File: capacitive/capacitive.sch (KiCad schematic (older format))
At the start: 66 parts, among them J101 UL, J102 UART, J103 SWD, J104 TX_PADS, J105 RX_PAD, J106 POWER, J107 UR, J108 LL, J109 LR, Q101 RU1C002ZPTCL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

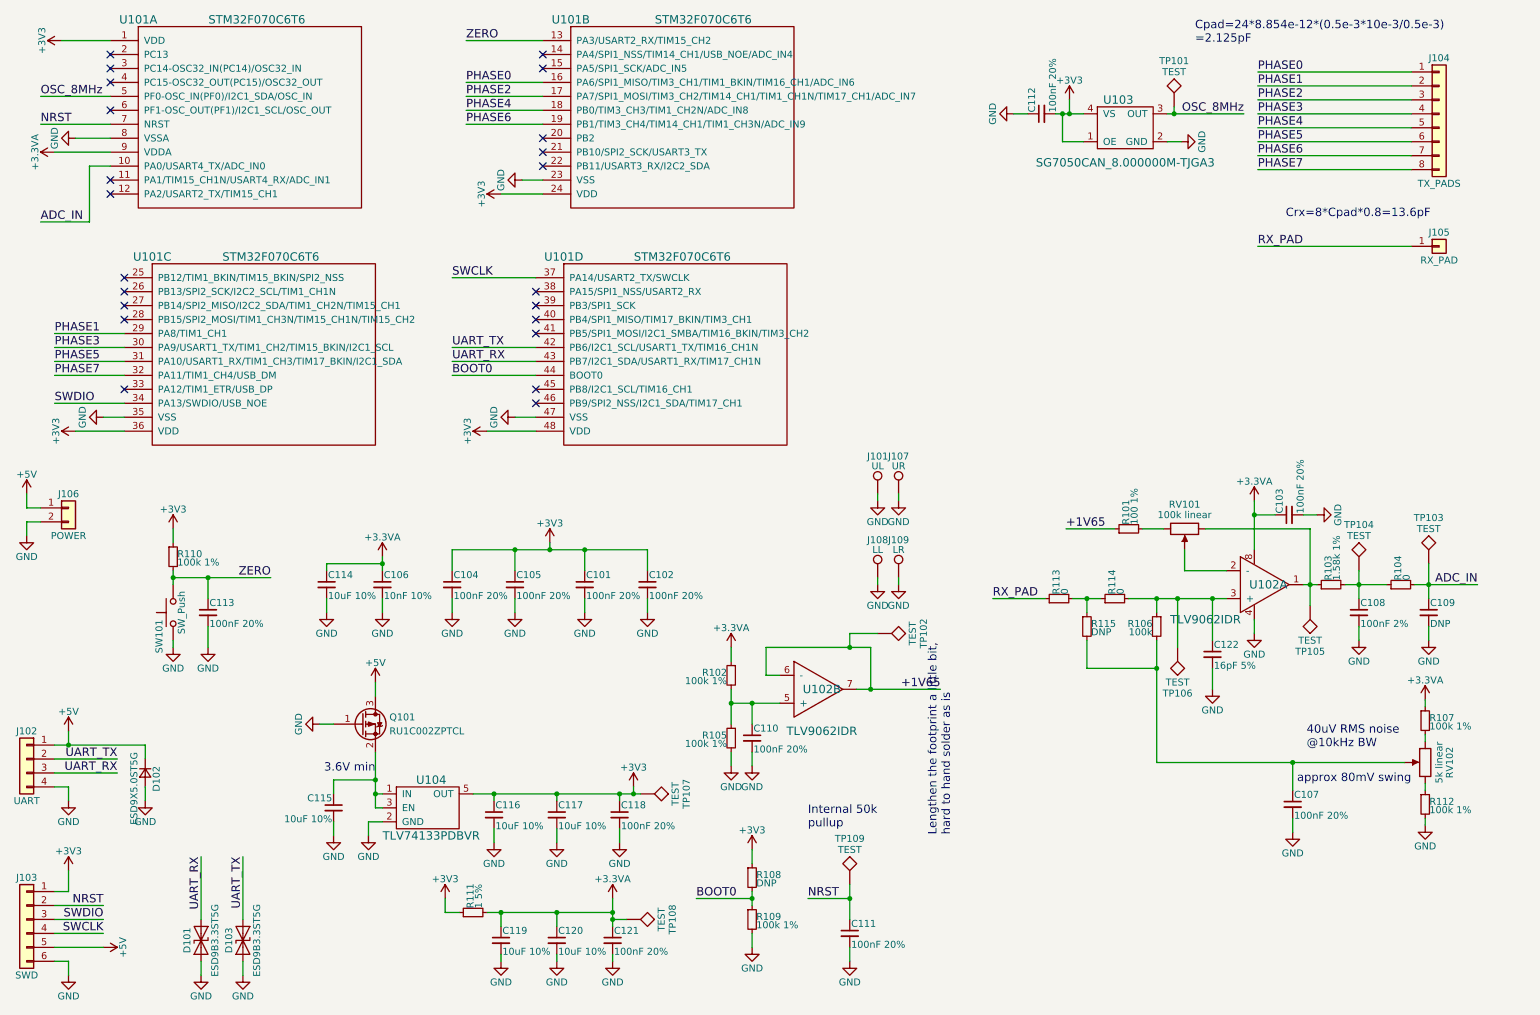
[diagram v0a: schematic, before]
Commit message: Add second stage of filtering
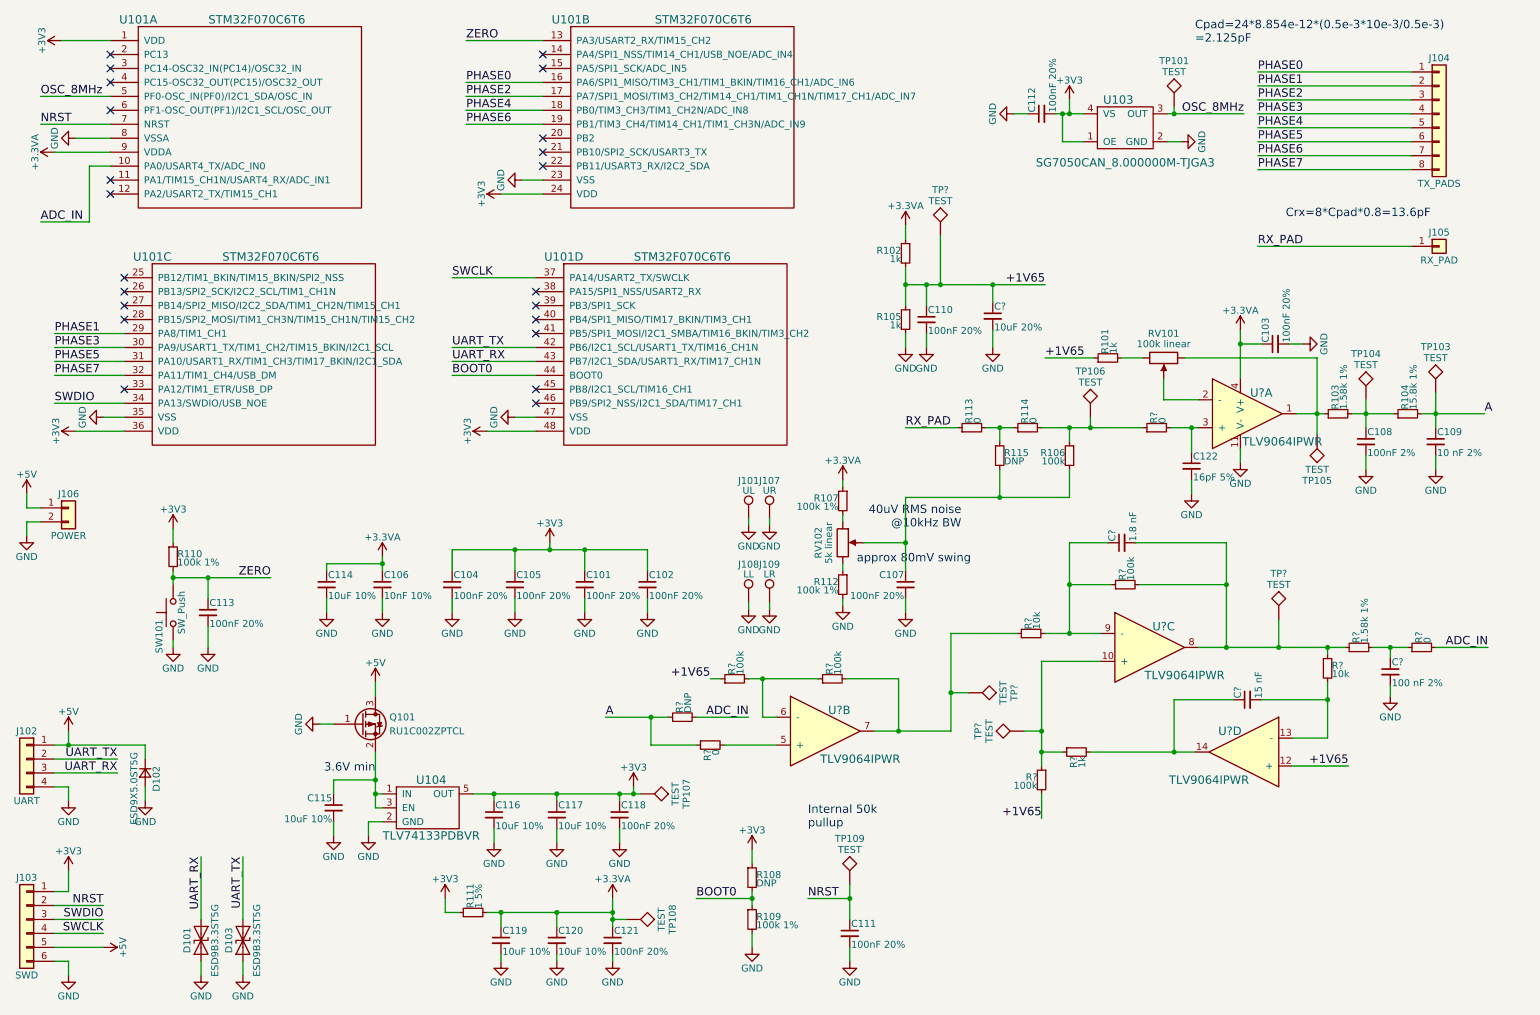
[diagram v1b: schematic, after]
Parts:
- removed TP102: TEST, Measurement_Points:Measurement_Point_Round-SMD-Pad_Small, symbol TEST
- removed U102: TLV9062IDR, capacitive:TI_SOIC-8, symbol TLV9062IDR
- added C?: 1.8 nF, symbol C_Small
- added C?: 15 nF, symbol C_Small
- added C?: 100 nF 2%, symbol C_Small
- added C?: 10uF 20%, Capacitors_SMD:C_0805_HandSoldering, symbol C_Small
- added R?: 0, Resistors_SMD:R_0805_HandSoldering, symbol R_Small
- added R?: 1k, symbol R_Small
- added R? (x4): 100k, symbol R_Small
- added R? (x2): 10k, symbol R_Small
- added R?: 1.58k 1%, symbol R_Small
- added R? (x2): 0, symbol R_Small
- added R?: DNP, symbol R_Small
- added TP?: TEST, symbol TEST
- added TP? (x3): TEST, Measurement_Points:Measurement_Point_Round-SMD-Pad_Small, symbol TEST
- added U? (x4): TLV9064IPWR, symbol TLV9064IPWR
- C109: value DNP -> 10 nF 2%
- R101: value 100 1% -> 1k
- R102, R105: value 100k 1% -> 1k
- R104: value 0 -> 15.8k 1%
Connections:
- net +1V65: now also C110.1, R102.2, R105.1, C?.1, R?.1, R?.2, TP?.1, U?.12 (+)
- net +3.3VA: now also U?.4 (V+)
- net ADC_IN: now also R?.2, R?.2; no longer C109.1, R104.2, TP103.1
- net GND: now also C?.2, C?.2, U?.11 (V-)
- net at R103.1, RV101.1, TP105.1: now also U?.1
- net at RV101.2: now also U?.2 (-)
- net at R106.1, R114.2, TP106.1: now also R?.1; no longer C122.1
- new net: C122.1, R?.2, U?.3 (+)
- new net: R?.2, U?.5 (+)
- new net: R?.1, R?.2, U?.6 (-)
- new net: R?.1, R?.2, TP?.1, U?.7
- new net: R?.1, R?.1, TP?.1, U?.10 (+)
- new net: C?.2, R?.1, R?.1, R?.2, TP?.1, U?.8
- new net: C?.1, R?.1, R?.2, U?.9 (-)
- new net: C?.2, R?.2, U?.13 (-)
- new net: C?.1, R?.2, U?.14
- new net: C?.1, R?.1, R?.2
- new net A: C109.1, R104.2, R?.1, R?.1, TP103.1
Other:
- note removed: "Lengthen the footprint a little bit,\nhard to hand solder as is"
- moved on the sheet: C103, C107, C108, C109, C110, C122, J101, J107, J108, J109, R101, R102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

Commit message: Save before autofill
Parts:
- C122: value 16pF 5% -> DNP; Mouser 81-GCM1885C1H160FA6J -> NoPart
- C123: renamed from C?; value 10uF 20% -> 10uF 10%
- R102, R105: value 1k -> 1k 1%; footprint Resistors_SMD:R_1206_HandSoldering -> Resistors_SMD:R_0402; Mouser 71-CRCW1206100KFKEAC -> 71-CRCW04021K00FKEDC
- R106: value 100k -> 100k 1%
- R117, R122, R123, R127: renamed from R?; value 100k -> 100k 1%
- R118: renamed from R?; value 10k -> 10k 1%; footprint (none) -> Resistors_SMD:R_0402; Mouser (none) -> 71-CRCW040210K0FKEDC
- R121: renamed from R?; value 10k -> 10k 1%
- R126: renamed from R?; value 1k -> 1k 1%
- U102: renamed from U?; footprint (none) -> capacitive:TI_TSSOP14; Mouser (none) -> 595-TLV9064IPWR
- gave numbers to parts that had none: 13
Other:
- note removed: "40uV RMS noise\n@10kHz BW"
- moved on the sheet: C124

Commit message: Autofill first time
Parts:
- R106, R117, R122, R123, R127: footprint (none) -> Resistors_SMD:R_1206_HandSoldering; Mouser (none) -> 71-CRCW1206100KFKEAC
- R108: Mouser (none) -> 71-RCS06030000Z0EA
- R119: footprint (none) -> Resistors_SMD:R_0603_HandSoldering; Mouser (none) -> 660-RN73H1JTD1581D25
- R120, R125: footprint (none) -> Resistors_SMD:R_0805_HandSoldering; Mouser (none) -> 71-CRCW12060000Z0EAC
- R121: footprint (none) -> Resistors_SMD:R_0402; Mouser (none) -> 71-CRCW040210K0FKEDC
- R124: footprint (none) -> Resistors_SMD:R_0603_HandSoldering; Mouser (none) -> 71-RCS06030000Z0EA
- R126: footprint (none) -> Resistors_SMD:R_0402; Mouser (none) -> 71-CRCW04021K00FKEDC
- TP102: footprint (none) -> Measurement_Points:Measurement_Point_Round-SMD-Pad_Small; Mouser (none) -> NoPart
- U102: footprint (none) -> capacitive:TI_TSSOP14; Mouser (none) -> 595-TLV9064IPWR
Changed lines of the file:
@@
 F 2 "Resistors_SMD:R_0603_HandSoldering" H 5850 6750 50  0001 C CNN
 F 3 "" H 5850 6750 50  0001 C CNN
+F 4 "71-RCS06030000Z0EA" H 5850 6750 50  0001 C "Mouser"
 	1    5850 6750
 	1    0    0    -1
@@
 F 0 "R106" H 8155 3745 50  0000 L CNN
 F 1 "100k 1%" H 8155 3685 50  0000 L CNN
-F 2 "" H 8125 3725 50  0001 C CNN
+F 2 "Resistors_SMD:R_1206_HandSoldering" H 8125 3725 50  0001 C CNN
 F 3 "" H 8125 3725 50  0001 C CNN
+F 4 "71-CRCW1206100KFKEAC" H 8125 3725 50  0001 C "Mouser"
 	1    8125 3725
 	1    0    0    -1
@@
 F 0 "TP102" H 7200 2450 50  0000 C BNN
 F 1 "TEST" H 7200 2400 50  0000 C CNN
-F 2 "" H 7200 2150 50  0001 C CNN
+F 2 "Measurement_Points:Measurement_Point_Round-SMD-Pad_Small" H 7200 2150 50  0001 C CNN
 F 3 "" H 7200 2150 50  0001 C CNN
+F 4 "NoPart" H 7200 2150 50  0001 C "Mouser"
 	1    7200 2150
 	1    0    0    -1
@@
 F 0 "U102" H 6475 5850 60  0000 C CNN
 F 1 "TLV9064IPWR" H 6625 5500 60  0000 C CNN
-F 2 "" H 6375 5700 60  0001 C CNN
+F 2 "capacitive:TI_TSSOP14" H 6375 5700 60  0001 C CNN
 F 3 "" H 6375 5700 60  0001 C CNN
+F 4 "595-TLV9064IPWR" H 6375 5700 60  0001 C "Mouser"
 	2    6375 5700
 	1    0    0    -1
@@
 F 0 "U102" H 8800 5250 60  0000 C CNN
 F 1 "TLV9064IPWR" H 8950 4900 60  0000 C CNN
-F 2 "" H 8700 5100 60  0001 C CNN
+F 2 "capacitive:TI_TSSOP14" H 8700 5100 60  0001 C CNN
 F 3 "" H 8700 5100 60  0001 C CNN
+F 4 "595-TLV9064IPWR" H 8700 5100 60  0001 C "Mouser"
 	3    8700 5100
 	1    0    0    -1
@@
 F 0 "R126" H 8205 5870 50  0000 L CNN
 F 1 "1k 1%" H 8205 5810 50  0000 L CNN
-F 2 "" H 8175 5850 50  0001 C CNN
+F 2 "Resistors_SMD:R_0402" H 8175 5850 50  0001 C CNN
 F 3 "" H 8175 5850 50  0001 C CNN
+F 4 "71-CRCW04021K00FKEDC" H 8175 5850 50  0001 C "Mouser"
 	1    8175 5850
 	0    -1   1    0
@@
 F 0 "R127" H 7955 6070 50  0000 L CNN
 F 1 "100k 1%" H 7955 6010 50  0000 L CNN
-F 2 "" H 7925 6050 50  0001 C CNN
+F 2 "Resistors_SMD:R_1206_HandSoldering" H 7925 6050 50  0001 C CNN
 F 3 "" H 7925 6050 50  0001 C CNN
+F 4 "71-CRCW1206100KFKEAC" H 7925 6050 50  0001 C "Mouser"
 	1    7925 6050
 	-1   0    0    -1
@@
 F 0 "R117" H 8555 4670 50  0000 L CNN
 F 1 "100k 1%" H 8555 4610 50  0000 L CNN
-F 2 "" H 8525 4650 50  0001 C CNN
+F 2 "Resistors_SMD:R_1206_HandSoldering" H 8525 4650 50  0001 C CNN
 F 3 "" H 8525 4650 50  0001 C CNN
+F 4 "71-CRCW1206100KFKEAC" H 8525 4650 50  0001 C "Mouser"
 	1    8525 4650
 	0    -1   -1   0
@@
 F 0 "U102" H 9475 6000 60  0000 C CNN
 F 1 "TLV9064IPWR" H 9625 5650 60  0000 C CNN
-F 2 "" H 9375 5850 60  0001 C CNN
+F 2 "capacitive:TI_TSSOP14" H 9375 5850 60  0001 C CNN
 F 3 "" H 9375 5850 60  0001 C CNN
+F 4 "595-TLV9064IPWR" H 9375 5850 60  0001 C "Mouser"
 	4    9375 5850
 	-1   0    0    -1
@@
 F 0 "R121" H 10005 5270 50  0000 L CNN
 F 1 "10k 1%" H 10005 5210 50  0000 L CNN
-F 2 "" H 9975 5250 50  0001 C CNN
+F 2 "Resistors_SMD:R_0402" H 9975 5250 50  0001 C CNN
 F 3 "" H 9975 5250 50  0001 C CNN
+F 4 "71-CRCW040210K0FKEDC" H 9975 5250 50  0001 C "Mouser"
 	1    9975 5250
 	1    0    0    -1
@@
 F 0 "R119" H 10230 5120 50  0000 L CNN
 F 1 "1.58k 1%" H 10230 5060 50  0000 L CNN
-F 2 "" H 10200 5100 50  0001 C CNN
+F 2 "Resistors_SMD:R_0603_HandSoldering" H 10200 5100 50  0001 C CNN
 F 3 "" H 10200 5100 50  0001 C CNN
+F 4 "660-RN73H1JTD1581D25" H 10200 5100 50  0001 C "Mouser"
 	1    10200 5100
 	0    -1   -1   0
@@
 F 0 "R125" H 5580 5820 50  0000 L CNN
 F 1 "0" H 5580 5760 50  0000 L CNN
-F 2 "" H 5550 5800 50  0001 C CNN
+F 2 "Resistors_SMD:R_0805_HandSoldering" H 5550 5800 50  0001 C CNN
 F 3 "" H 5550 5800 50  0001 C CNN
+F 4 "71-CRCW12060000Z0EAC" H 5550 5800 50  0001 C "Mouser"
 	1    5550 5800
 	0    -1   1    0
@@
 F 0 "R124" H 5380 5620 50  0000 L CNN
 F 1 "DNP" H 5380 5560 50  0000 L CNN
-F 2 "" H 5350 5600 50  0001 C CNN
+F 2 "Resistors_SMD:R_0603_HandSoldering" H 5350 5600 50  0001 C CNN
 F 3 "" H 5350 5600 50  0001 C CNN
+F 4 "71-RCS06030000Z0EA" H 5350 5600 50  0001 C "Mouser"
 	1    5350 5600
 	0    -1   -1   0
@@
 F 0 "R123" H 6455 5345 50  0000 L CNN
 F 1 "100k 1%" H 6455 5285 50  0000 L CNN
-F 2 "" H 6425 5325 50  0001 C CNN
+F 2 "Resistors_SMD:R_1206_HandSoldering" H 6425 5325 50  0001 C CNN
 F 3 "" H 6425 5325 50  0001 C CNN
+F 4 "71-CRCW1206100KFKEAC" H 6425 5325 50  0001 C "Mouser"
 	1    6425 5325
 	0    -1   -1   0
@@
 F 0 "R122" H 5755 5345 50  0000 L CNN
 F 1 "100k 1%" H 5755 5285 50  0000 L CNN
-F 2 "" H 5725 5325 50  0001 C CNN
+F 2 "Resistors_SMD:R_1206_HandSoldering" H 5725 5325 50  0001 C CNN
 F 3 "" H 5725 5325 50  0001 C CNN
+F 4 "71-CRCW1206100KFKEAC" H 5725 5325 50  0001 C "Mouser"
 	1    5725 5325
 	0    -1   -1   0
@@
 F 0 "R120" H 10680 5120 50  0000 L CNN
 F 1 "0" H 10680 5060 50  0000 L CNN
-F 2 "" H 10650 5100 50  0001 C CNN
+F 2 "Resistors_SMD:R_0805_HandSoldering" H 10650 5100 50  0001 C CNN
 F 3 "" H 10650 5100 50  0001 C CNN
+F 4 "71-CRCW12060000Z0EAC" H 10650 5100 50  0001 C "Mouser"
 	1    10650 5100
 	0    -1   -1   0

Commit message: Save before autofill
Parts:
- added C?: 33nF 5%, Capacitors_SMD:C_0603_HandSoldering, symbol C_Small
- C109: Mouser NoPart -> 81-GRM2195C1H103FA1D
- C124: value 1.8 nF -> 1.8nF 2%; footprint (none) -> Capacitors_SMD:C_0603_HandSoldering; Mouser (none) -> 81-GRM1885C1H182GA1D
- C125: value 100 nF 2% -> 100nF 2%
- C126: value 15 nF -> 33nF 5%
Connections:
- net at R126.2, U102.14: now also C?.1; no longer C126.1
- new net: C126.1, C?.2
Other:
- moved on the sheet: C126
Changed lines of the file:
@@
 F 2 "Capacitors_SMD:C_0805_HandSoldering" H 10750 3625 50  0001 C CNN
 F 3 "" H 10750 3625 50  0001 C CNN
-F 4 "NoPart" H 10750 3625 60  0001 C CNN "Mouser"
+F 4 "81-GRM2195C1H103FA1D" H 10750 3625 60  0001 C CNN "Mouser"
 	1    10750 3625
 	1    0    0    -1
@@
 F 2 "Resistors_SMD:R_0603_HandSoldering" H 5850 6750 50  0001 C CNN
 F 3 "" H 5850 6750 50  0001 C CNN
-F 4 "71-RCS06030000Z0EA" H 5850 6750 50  0001 C "Mouser"
+F 4 "71-RCS06030000Z0EA" H 5850 6750 50  0001 C CNN "Mouser"
 	1    5850 6750
 	1    0    0    -1
@@
 F 2 "Resistors_SMD:R_1206_HandSoldering" H 8125 3725 50  0001 C CNN
 F 3 "" H 8125 3725 50  0001 C CNN
-F 4 "71-CRCW1206100KFKEAC" H 8125 3725 50  0001 C "Mouser"
+F 4 "71-CRCW1206100KFKEAC" H 8125 3725 50  0001 C CNN "Mouser"
 	1    8125 3725
 	1    0    0    -1
@@
 F 2 "Measurement_Points:Measurement_Point_Round-SMD-Pad_Small" H 7200 2150 50  0001 C CNN
 F 3 "" H 7200 2150 50  0001 C CNN
-F 4 "NoPart" H 7200 2150 50  0001 C "Mouser"
+F 4 "NoPart" H 7200 2150 50  0001 C CNN "Mouser"
 	1    7200 2150
 	1    0    0    -1
@@
 F 2 "capacitive:TI_TSSOP14" H 6375 5700 60  0001 C CNN
 F 3 "" H 6375 5700 60  0001 C CNN
-F 4 "595-TLV9064IPWR" H 6375 5700 60  0001 C "Mouser"
+F 4 "595-TLV9064IPWR" H 6375 5700 60  0001 C CNN "Mouser"
 	2    6375 5700
 	1    0    0    -1
@@
 F 2 "capacitive:TI_TSSOP14" H 8700 5100 60  0001 C CNN
 F 3 "" H 8700 5100 60  0001 C CNN
-F 4 "595-TLV9064IPWR" H 8700 5100 60  0001 C "Mouser"
+F 4 "595-TLV9064IPWR" H 8700 5100 60  0001 C CNN "Mouser"
 	3    8700 5100
 	1    0    0    -1
@@
 F 2 "Resistors_SMD:R_0402" H 8175 5850 50  0001 C CNN
 F 3 "" H 8175 5850 50  0001 C CNN
-F 4 "71-CRCW04021K00FKEDC" H 8175 5850 50  0001 C "Mouser"
+F 4 "71-CRCW04021K00FKEDC" H 8175 5850 50  0001 C CNN "Mouser"
 	1    8175 5850
 	0    -1   1    0
@@
 F 2 "Resistors_SMD:R_1206_HandSoldering" H 7925 6050 50  0001 C CNN
 F 3 "" H 7925 6050 50  0001 C CNN
-F 4 "71-CRCW1206100KFKEAC" H 7925 6050 50  0001 C "Mouser"
+F 4 "71-CRCW1206100KFKEAC" H 7925 6050 50  0001 C CNN "Mouser"
 	1    7925 6050
 	-1   0    0    -1
@@
 F 2 "Resistors_SMD:R_1206_HandSoldering" H 8525 4650 50  0001 C CNN
 F 3 "" H 8525 4650 50  0001 C CNN
-F 4 "71-CRCW1206100KFKEAC" H 8525 4650 50  0001 C "Mouser"
+F 4 "71-CRCW1206100KFKEAC" H 8525 4650 50  0001 C CNN "Mouser"
 	1    8525 4650
 	0    -1   -1   0
@@
 P 8500 4275
 F 0 "C124" H 8510 4345 50  0000 L CNN
-F 1 "1.8 nF" H 8510 4195 50  0000 L CNN
-F 2 "" H 8500 4275 50  0001 C CNN
+F 1 "1.8nF 2%" H 8510 4195 50  0000 L CNN
+F 2 "Capacitors_SMD:C_0603_HandSoldering" H 8500 4275 50  0001 C CNN
 F 3 "" H 8500 4275 50  0001 C CNN
+F 4 "81-GRM1885C1H182GA1D" H 8500 4275 60  0001 C CNN "Mouser"
 	1    8500 4275
 	0    -1   -1   0
@@
 F 2 "capacitive:TI_TSSOP14" H 9375 5850 60  0001 C CNN
 F 3 "" H 9375 5850 60  0001 C CNN
-F 4 "595-TLV9064IPWR" H 9375 5850 60  0001 C "Mouser"
+F 4 "595-TLV9064IPWR" H 9375 5850 60  0001 C CNN "Mouser"
 	4    9375 5850
 	-1   0    0    -1
@@
 L C_Small C126
 U 1 1 5B529C7A
-P 9400 5475
-F 0 "C126" H 9410 5545 50  0000 L CNN
-F 1 "15 nF" H 9410 5395 50  0000 L CNN
-F 2 "" H 9400 5475 50  0001 C CNN
-F 3 "" H 9400 5475 50  0001 C CNN
-	1    9400 5475
+P 9725 5475
+F 0 "C126" H 9735 5545 50  0000 L CNN
+F 1 "33nF 5%" H 9735 5395 50  0000 L CNN
+F 2 "" H 9725 5475 50  0001 C CNN
+F 3 "" H 9725 5475 50  0001 C CNN
+	1    9725 5475
 	0    -1   -1   0
 $EndComp
@@
 F 2 "Resistors_SMD:R_0402" H 9975 5250 50  0001 C CNN
 F 3 "" H 9975 5250 50  0001 C CNN
-F 4 "71-CRCW040210K0FKEDC" H 9975 5250 50  0001 C "Mouser"
+F 4 "71-CRCW040210K0FKEDC" H 9975 5250 50  0001 C CNN "Mouser"
 	1    9975 5250
 	1    0    0    -1
@@
 	9975 5750 9725 5750
 Wire Wire Line
-	9500 5475 9975 5475
+	9825 5475 9975 5475
 Connection ~ 9975 5475
-Wire Wire Line
-	9300 5475 8875 5475
 Wire Wire Line
 	8875 5475 8875 5850
@@
 F 2 "Resistors_SMD:R_0603_HandSoldering" H 10200 5100 50  0001 C CNN
 F 3 "" H 10200 5100 50  0001 C CNN
-F 4 "660-RN73H1JTD1581D25" H 10200 5100 50  0001 C "Mouser"
+F 4 "660-RN73H1JTD1581D25" H 10200 5100 50  0001 C CNN "Mouser"
 	1    10200 5100
 	0    -1   -1   0
@@
 P 10425 5275
 F 0 "C125" H 10435 5345 50  0000 L CNN
-F 1 "100 nF 2%" H 10435 5195 50  0000 L CNN
+F 1 "100nF 2%" H 10435 5195 50  0000 L CNN
 F 2 "" H 10425 5275 50  0001 C CNN
 F 3 "" H 10425 5275 50  0001 C CNN
@@
 F 2 "Resistors_SMD:R_0805_HandSoldering" H 5550 5800 50  0001 C CNN
 F 3 "" H 5550 5800 50  0001 C CNN
-F 4 "71-CRCW12060000Z0EAC" H 5550 5800 50  0001 C "Mouser"
+F 4 "71-CRCW12060000Z0EAC" H 5550 5800 50  0001 C CNN "Mouser"
 	1    5550 5800
 	0    -1   1    0
@@
 F 2 "Resistors_SMD:R_0603_HandSoldering" H 5350 5600 50  0001 C CNN
 F 3 "" H 5350 5600 50  0001 C CNN
-F 4 "71-RCS06030000Z0EA" H 5350 5600 50  0001 C "Mouser"
+F 4 "71-RCS06030000Z0EA" H 5350 5600 50  0001 C CNN "Mouser"
 	1    5350 5600
 	0    -1   -1   0
@@
 F 2 "Resistors_SMD:R_1206_HandSoldering" H 6425 5325 50  0001 C CNN
 F 3 "" H 6425 5325 50  0001 C CNN
-F 4 "71-CRCW1206100KFKEAC" H 6425 5325 50  0001 C "Mouser"
+F 4 "71-CRCW1206100KFKEAC" H 6425 5325 50  0001 C CNN "Mouser"
 	1    6425 5325
 	0    -1   -1   0
@@
 F 2 "Resistors_SMD:R_1206_HandSoldering" H 5725 5325 50  0001 C CNN
 F 3 "" H 5725 5325 50  0001 C CNN
-F 4 "71-CRCW1206100KFKEAC" H 5725 5325 50  0001 C "Mouser"
+F 4 "71-CRCW1206100KFKEAC" H 5725 5325 50  0001 C CNN "Mouser"
 	1    5725 5325
 	0    -1   -1   0
@@
 F 2 "Resistors_SMD:R_0805_HandSoldering" H 10650 5100 50  0001 C CNN
 F 3 "" H 10650 5100 50  0001 C CNN
-F 4 "71-CRCW12060000Z0EAC" H 10650 5100 50  0001 C "Mouser"
+F 4 "71-CRCW12060000Z0EAC" H 10650 5100 50  0001 C CNN "Mouser"
 	1    10650 5100
 	0    -1   -1   0
@@
 	4275 6900 4275 7000
 Connection ~ 4275 7000
+$Comp
+L C_Small C?
+U 1 1 5B525D68
+P 9400 5475
+F 0 "C?" H 9410 5545 50  0000 L CNN
+F 1 "33nF 5%" H 9410 5395 50  0000 L CNN
+F 2 "Capacitors_SMD:C_0603_HandSoldering" H 9400 5475 50  0001 C CNN
+F 3 "" H 9400 5475 50  0001 C CNN
+F 4 "80-C0603C333J4RECLR" H 9400 5475 60  0001 C CNN "Mouser"
+	1    9400 5475
+	0    -1   -1   0
+$EndComp
+Wire Wire Line
+	9500 5475 9625 5475
+Wire Wire Line
+	9300 5475 8875 5475
 $EndSCHEMATC

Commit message: All parts sourced and netlist generated
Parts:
- C125: footprint (none) -> Capacitors_SMD:C_1210_HandSoldering; Mouser (none) -> 667-ECH-U1C104GX5
- C126: footprint (none) -> Capacitors_SMD:C_0603_HandSoldering; Mouser (none) -> 80-C0603C333J4RECLR
- gave numbers to parts that had none: 1
